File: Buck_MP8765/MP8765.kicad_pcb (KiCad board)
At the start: 2 copper layers, 40 x 20 mm, 28 parts, among them J1 Jumper

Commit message: ...
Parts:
- DA1: footprint QFN,_DFN,_LGA:FCQFN16 -> QFN,_DFN,_LGA:HFCQFN16
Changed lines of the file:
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@@
-(kicad_pcb (version 20171130) (host pcbnew "(5.0.0-rc2-dev-596-gcfd2f1d00)")
+(kicad_pcb (version 20171130) (host pcbnew "(5.1.5)-1")
   (general
     (thickness 1.6)
@@
     (zone_45_only no)
     (trace_min 0.2)
-    (segment_width 0.15)
-    (edge_width 0.15)
     (via_size 0.7)
     (via_drill 0.3)
@@
     (uvia_min_size 0.508)
     (uvia_min_drill 0.127)
+    (edge_width 0.15)
+    (segment_width 0.15)
     (pcb_text_width 0.3)
     (pcb_text_size 1.5 1.5)
@@
       (hpglpennumber 1)
       (hpglpenspeed 20)
-      (hpglpendiameter 15)
+      (hpglpendiameter 15.000000)
       (psnegative false)
       (psa4output false)
@@
       (drillshape 0)
       (scaleselection 1)
-      (outputdirectory Gerber/))
+      (outputdirectory "Gerber/"))
   )
   (net 0 "")
@@
     (uvia_dia 0.7)
     (uvia_drill 0.3)
+    (diff_pair_width 0.2)
     (diff_pair_gap 0.2)
-    (diff_pair_width 0.2)
     (add_net +5Vout)
     (add_net /5Vout_Good)
@@
     (uvia_dia 0.7)
     (uvia_drill 0.3)
+    (diff_pair_width 0.2)
     (diff_pair_gap 0.2)
-    (diff_pair_width 0.2)
     (add_net GND)
     (add_net GNDL1)
@@
     (uvia_dia 0.7)
     (uvia_drill 0.3)
+    (diff_pair_width 0.2)
     (diff_pair_gap 0.2)
-    (diff_pair_width 0.2)
   )
   (net_class wide1.0 ""
@@
     (uvia_dia 0.7)
     (uvia_drill 0.3)
+    (diff_pair_width 0.2)
     (diff_pair_gap 0.2)
-    (diff_pair_width 0.2)
   )
   (net_class wide1.5 ""
@@
     (uvia_dia 0.7)
     (uvia_drill 0.3)
+    (diff_pair_width 0.2)
     (diff_pair_gap 0.2)
-    (diff_pair_width 0.2)
     (add_net +12V)
     (add_net /+SW1)
@@
     (uvia_dia 0.7)
     (uvia_drill 0.3)
+    (diff_pair_width 0.2)
     (diff_pair_gap 0.2)
-    (diff_pair_width 0.2)
   )
   (net_class wide4.0 ""
@@
     (uvia_dia 0.7)
     (uvia_drill 0.3)
+    (diff_pair_width 0.2)
     (diff_pair_gap 0.2)
-    (diff_pair_width 0.2)
   )
   (module Capacitors:CAP0603 (layer F.Cu)
@@
       (rotate (xyz 0 0 0))
     )
-  )
-  (module QFN,_DFN,_LGA:FCQFN16 (layer F.Cu)
-    (at 115.375 60.375)
-    (attr smd)
-    (fp_text reference DA1 (at 0 3.2) (layer F.SilkS)
-      (effects (font (size 0.6 0.6) (thickness 0.15)))
-    )
-    (fp_text value MP8765 (at 0 -3.2) (layer F.SilkS)
-      (effects (font (size 0.6 0.6) (thickness 0.15)))
-    )
-    (fp_line (start -1.5 -1.5) (end 1.5 -1.5) (layer F.SilkS) (width 0.15))
-    (fp_line (start -1.5 1.5) (end -1.5 -1.5) (layer F.SilkS) (width 0.15))
-    (fp_line (start 1.5 1.5) (end -1.5 1.5) (layer F.SilkS) (width 0.15))
-    (fp_line (start 1.5 -1.5) (end 1.5 1.5) (layer F.SilkS) (width 0.15))
-    (fp_line (start -0.9 -1.5) (end -1.5 -0.9) (layer F.SilkS) (width 0.15))
-    (fp_line (start -2.5 2.5) (end -2.5 -2.5) (layer F.SilkS) (width 0.15))
-    (fp_line (start 2.5 2.5) (end -2.5 2.5) (layer F.SilkS) (width 0.15))
-    (fp_line (start 2.5 -2.5) (end 2.5 2.5) (layer F.SilkS) (width 0.15))
-    (fp_line (start -2.5 -2.5) (end 2.5 -2.5) (layer F.SilkS) (width 0.15))
-    (fp_line (start -1.5 -2.5) (end -2.5 -1.5) (layer F.SilkS) (width 0.15))
-    (fp_line (start -1.5 -1.3) (end -1.3 -1.5) (layer F.SilkS) (width 0.15))
-    (fp_line (start -1.5 -1.1) (end -1.1 -1.5) (layer F.SilkS) (width 0.15))
-    (pad 15 smd rect (at 0 -0.165) (size 0.65 0.3) (layers F.Cu F.Paste F.Mask))
-    (pad 16 smd rect (at 0 0.435) (size 0.65 0.3) (layers F.Cu F.Paste F.Mask))
-    (pad 9 smd oval (at 1.35 -0.175) (size 1.3 0.3) (layers F.Cu F.Paste F.Mask)
-      (net 5 /+SW1))
-    (pad 8 smd oval (at 1.35 0.525) (size 1.3 0.3) (layers F.Cu F.Paste F.Mask)
-      (net 5 /+SW1))
-    (pad 5 smd oval (at 0 1.55 270) (size 0.9 0.2) (layers F.Cu F.Paste F.Mask))
-    (pad 2 smd oval (at -1.35 0.175) (size 1.3 0.3) (layers F.Cu F.Paste F.Mask)
-      (net 1 GND))
-    (pad 1 smd rect (at -1.35 -0.525) (size 1.3 0.3) (layers F.Cu F.Paste F.Mask)
-      (net 2 +12V))
-    (pad 4 smd oval (at -0.4 1.55 270) (size 0.9 0.2) (layers F.Cu F.Paste F.Mask)
-      (net 8 /5Vout_Good))
-    (pad 3 smd oval (at -0.8 1.55 270) (size 0.9 0.2) (layers F.Cu F.Paste F.Mask))
-    (pad 6 smd oval (at 0.4 1.55 270) (size 0.9 0.2) (layers F.Cu F.Paste F.Mask)
-      (net 6 GNDL1))
-    (pad 7 smd oval (at 0.8 1.55 270) (size 0.9 0.2) (layers F.Cu F.Paste F.Mask)
-      (net 7 +5Vout))
-    (pad 10 smd oval (at 0.8 -1.5 270) (size 0.9 0.2) (layers F.Cu F.Paste F.Mask)
-      (net 10 "Net-(DA1-Pad10)"))
-    (pad 11 smd oval (at 0.4 -1.5 270) (size 0.9 0.2) (layers F.Cu F.Paste F.Mask)
-      (net 3 "Net-(C5-Pad1)"))
-    (pad 14 smd oval (at -0.8 -1.5 270) (size 0.9 0.2) (layers F.Cu F.Paste F.Mask)
-      (net 6 GNDL1))
-    (pad 13 smd oval (at -0.4 -1.5 270) (size 0.9 0.2) (layers F.Cu F.Paste F.Mask)
-      (net 12 /Enadle))
-    (pad 12 smd oval (at 0 -1.5 270) (size 0.9 0.2) (layers F.Cu F.Paste F.Mask)
-      (net 11 "Net-(DA1-Pad12)"))
   )
   (module "Installation:Heatsink_14x13(18)x6.2" (layer B.Cu)
@@
     (fp_circle (center 0.3 0) (end 0.2 0) (layer B.SilkS) (width 0.15))
   )
+  (module QFN,_DFN,_LGA:HFCQFN16 (layer F.Cu)
+    (at 115.375 60.375)
+    (attr smd)
+    (fp_text reference DA1 (at 0 3.2) (layer F.SilkS)
+      (effects (font (size 0.6 0.6) (thickness 0.15)))
+    )
+    (fp_text value MP8765 (at 0 -3.2) (layer F.SilkS)
+      (effects (font (size 0.6 0.6) (thickness 0.15)))
+    )
+    (fp_line (start -1.5 -1.5) (end 1.5 -1.5) (layer F.SilkS) (width 0.15))
+    (fp_line (start -1.5 1.5) (end -1.5 -1.5) (layer F.SilkS) (width 0.15))
+    (fp_line (start 1.5 1.5) (end -1.5 1.5) (layer F.SilkS) (width 0.15))
+    (fp_line (start 1.5 -1.5) (end 1.5 1.5) (layer F.SilkS) (width 0.15))
+    (fp_line (start -0.9 -1.5) (end -1.5 -0.9) (layer F.SilkS) (width 0.15))
+    (fp_line (start -2.5 2.5) (end -2.5 -2.5) (layer F.SilkS) (width 0.15))
+    (fp_line (start 2.5 2.5) (end -2.5 2.5) (layer F.SilkS) (width 0.15))
+    (fp_line (start 2.5 -2.5) (end 2.5 2.5) (layer F.SilkS) (width 0.15))
+    (fp_line (start -2.5 -2.5) (end 2.5 -2.5) (layer F.SilkS) (width 0.15))
+    (fp_line (start -1.5 -2.5) (end -2.5 -1.5) (layer F.SilkS) (width 0.15))
+    (fp_line (start -1.5 -1.3) (end -1.3 -1.5) (layer F.SilkS) (width 0.15))
+    (fp_line (start -1.5 -1.1) (end -1.1 -1.5) (layer F.SilkS) (width 0.15))
+    (pad 15 smd rect (at 0 -0.165) (size 0.65 0.3) (layers F.Cu F.Paste F.Mask))
+    (pad 16 smd rect (at 0 0.435) (size 0.65 0.3) (layers F.Cu F.Paste F.Mask))
+    (pad 9 smd oval (at 1.35 -0.175) (size 1.3 0.3) (layers F.Cu F.Paste F.Mask)
+      (net 5 /+SW1))
+    (pad 8 smd oval (at 1.35 0.525) (size 1.3 0.3) (layers F.Cu F.Paste F.Mask)
+      (net 5 /+SW1))
+    (pad 5 smd oval (at 0 1.55 270) (size 0.9 0.2) (layers F.Cu F.Paste F.Mask))
+    (pad 2 smd oval (at -1.35 0.175) (size 1.3 0.3) (layers F.Cu F.Paste F.Mask)
+      (net 1 GND))
+    (pad 1 smd rect (at -1.35 -0.525) (size 1.3 0.3) (layers F.Cu F.Paste F.Mask)
+      (net 2 +12V))
+    (pad 4 smd oval (at -0.4 1.55 270) (size 0.9 0.2) (layers F.Cu F.Paste F.Mask)
+      (net 8 /5Vout_Good))
+    (pad 3 smd oval (at -0.8 1.55 270) (size 0.9 0.2) (layers F.Cu F.Paste F.Mask))
+    (pad 6 smd oval (at 0.4 1.55 270) (size 0.9 0.2) (layers F.Cu F.Paste F.Mask)
+      (net 6 GNDL1))
+    (pad 7 smd oval (at 0.8 1.55 270) (size 0.9 0.2) (layers F.Cu F.Paste F.Mask)
+      (net 7 +5Vout))
+    (pad 10 smd oval (at 0.8 -1.5 270) (size 0.9 0.2) (layers F.Cu F.Paste F.Mask)
+      (net 10 "Net-(DA1-Pad10)"))
+    (pad 11 smd oval (at 0.4 -1.5 270) (size 0.9 0.2) (layers F.Cu F.Paste F.Mask)
+      (net 3 "Net-(C5-Pad1)"))
+    (pad 14 smd oval (at -0.8 -1.5 270) (size 0.9 0.2) (layers F.Cu F.Paste F.Mask)
+      (net 6 GNDL1))
+    (pad 13 smd oval (at -0.4 -1.5 270) (size 0.9 0.2) (layers F.Cu F.Paste F.Mask)
+      (net 12 /Enadle))
+    (pad 12 smd oval (at 0 -1.5 270) (size 0.9 0.2) (layers F.Cu F.Paste F.Mask)
+      (net 11 "Net-(DA1-Pad12)"))
+    (pad 9 smd rect (at 0.8 0) (size 2.4 1.6) (layers F.Cu)
+      (net 5 /+SW1))
+  )
   (gr_line (start 100 70) (end 100 50) (angle 90) (layer Edge.Cuts) (width 0.15))

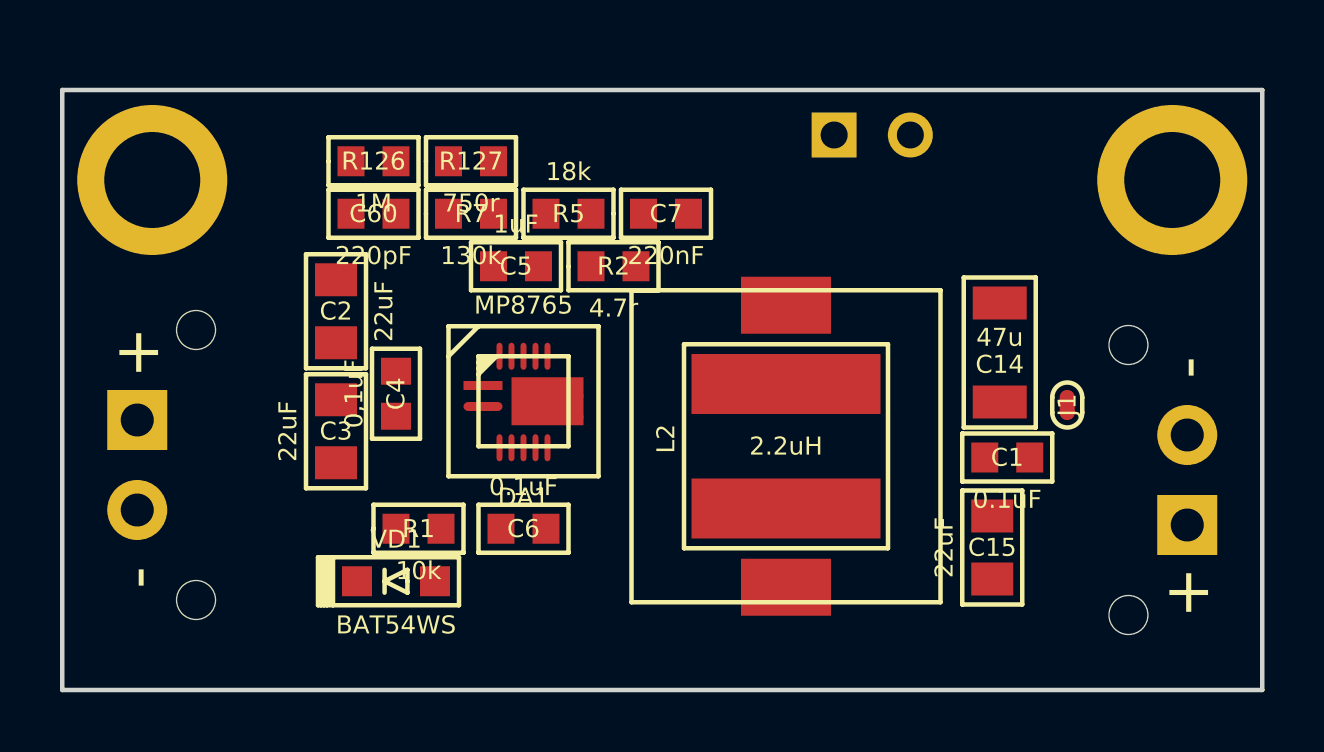
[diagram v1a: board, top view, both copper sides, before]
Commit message: модуль MP8765 завершён
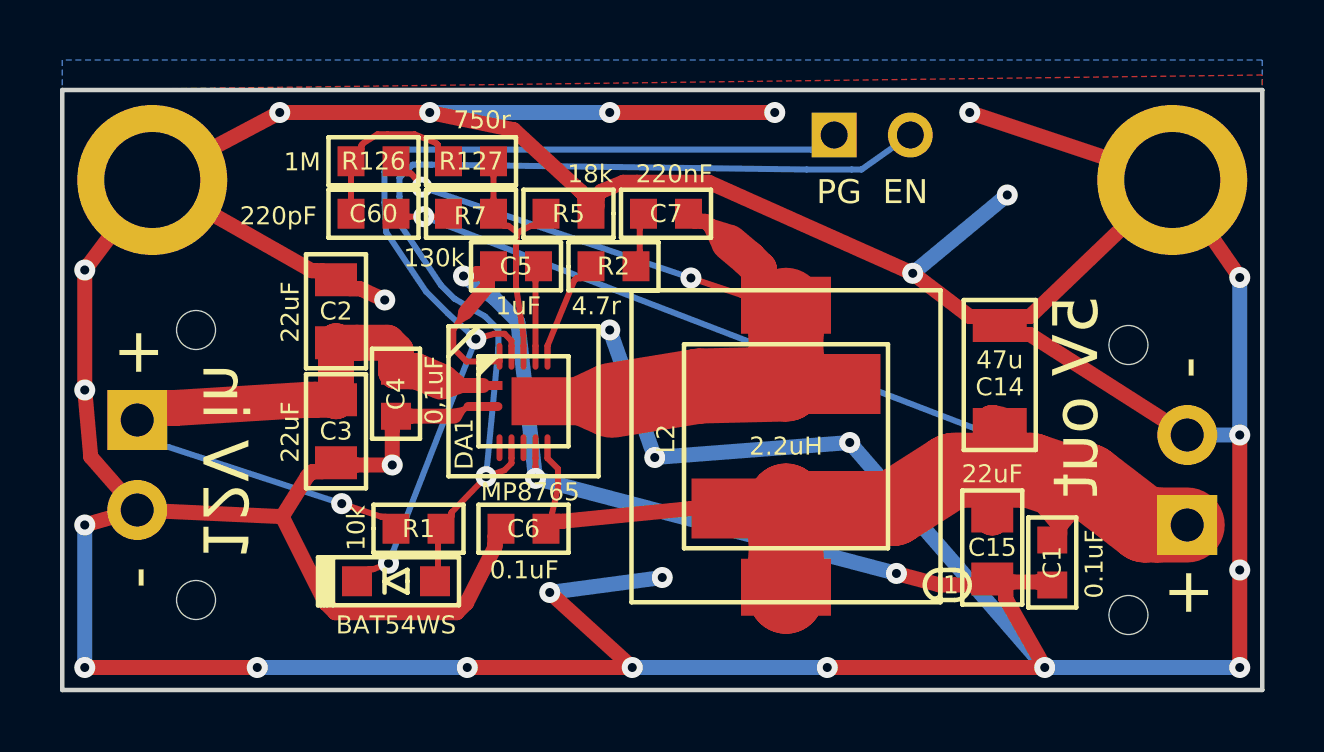
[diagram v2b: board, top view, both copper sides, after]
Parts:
- XP2: value 12V in -> 5V out (<6A)
- XP3: value PG EN -> PG EN
- moved J1 7.21 mm to (129.5, 66.5), turned to 0 degrees
- moved C1 3.81 mm to (133.0, 65.8), turned to 270 degrees
- moved C14 0.75 mm to (131.2, 59.5)
- moved Heat1 0.18 mm to (115.5, 60.5)
- turned R126 to 180 degrees
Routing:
- net GND: track 0.00 -> 215.6 mm, vias 0 -> 27
- net +5Vout: track 0.00 -> 69.3 mm, vias 0 -> 1
- net /+SW1: track 0.00 -> 37.8 mm, vias 0 -> 2
- net /5Vout_Good: track 0.00 -> 34.5 mm, vias 0 -> 1
- net /Enadle: track 0.00 -> 33.3 mm, vias 0 -> 2
- net GNDL1: track 0.00 -> 29.5 mm, vias 0 -> 3
- net +12V: track 0.00 -> 25.4 mm, vias 0 -> 1
- net Net-(DA1-Pad12): track 0.00 -> 8.14 mm
- net Net-(C60-Pad1): track 0.00 -> 5.84 mm
- net Net-(DA1-Pad10): track 0.00 -> 3.47 mm
- net Net-(C5-Pad1): track 0.00 -> 3.01 mm
- net Net-(C7-Pad1): track 0.00 -> 1.79 mm
- added copper zone on B.Cu, net GND
- added copper zone on F.Cu, net GND
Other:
- net class wide0.75 removed
- net class wide1.0 removed
- net class wide1.2 added: clearance 0.2, trace_width 1.2, via_dia 0.7, via_drill 0.3
- net class wide1.5 removed
- net class wide2.0 removed
- net class wide2.5 added: clearance 0.2, trace_width 2.5, via_dia 0.7, via_drill 0.3
- net class wide4.0 removed
- board text added: "12V in"
- board text added: "5V out"
- board text added: "MP8765 DC/DC module"
- board text added: "PG EN"
